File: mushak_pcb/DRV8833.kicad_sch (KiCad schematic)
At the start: 8 parts, among them U3 DRV8833PW

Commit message: Add footprints
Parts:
- C26, C27, C28: footprint (none) -> Capacitor_SMD:C_0805_2012Metric
- TP24, TP25, TP26: footprint (none) -> TestPoint:TestPoint_Pad_2.5x2.5mm
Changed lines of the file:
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@@
       (effects (font (size 1 1)) (justify left))
     )
-    (property "Footprint" "" (id 2) (at 194.31 113.03 0)
+    (property "Footprint" "TestPoint:TestPoint_Pad_2.5x2.5mm" (id 2) (at 194.31 113.03 0)
       (effects (font (size 1.27 1.27)) hide)
     )
@@
       (effects (font (size 1 1)) (justify left))
     )
-    (property "Footprint" "" (id 2) (at 194.31 107.95 0)
+    (property "Footprint" "TestPoint:TestPoint_Pad_2.5x2.5mm" (id 2) (at 194.31 107.95 0)
       (effects (font (size 1.27 1.27)) hide)
     )
@@
     (property "Reference" "C26" (id 0) (at 126.492 82.55 90))
     (property "Value" "10nF" (id 1) (at 126.492 85.09 90))
-    (property "Footprint" "" (id 2) (at 130.302 89.2048 0)
+    (property "Footprint" "Capacitor_SMD:C_0805_2012Metric" (id 2) (at 130.302 89.2048 0)
       (effects (font (size 1.27 1.27)) hide)
     )
@@
       (effects (font (size 1 1)) (justify left))
     )
-    (property "Footprint" "" (id 2) (at 194.31 110.49 0)
+    (property "Footprint" "TestPoint:TestPoint_Pad_2.5x2.5mm" (id 2) (at 194.31 110.49 0)
       (effects (font (size 1.27 1.27)) hide)
     )
@@
     (property "Reference" "C27" (id 0) (at 143.764 68.58 90))
     (property "Value" "2.2uF" (id 1) (at 143.764 71.12 90))
-    (property "Footprint" "" (id 2) (at 147.574 74.7268 0)
+    (property "Footprint" "Capacitor_SMD:C_0805_2012Metric" (id 2) (at 147.574 74.7268 0)
       (effects (font (size 1.27 1.27)) hide)
     )
@@
     (property "Reference" "C28" (id 0) (at 163.322 68.58 90))
     (property "Value" "10uF" (id 1) (at 163.322 71.12 90))
-    (property "Footprint" "" (id 2) (at 167.132 74.7268 0)
+    (property "Footprint" "Capacitor_SMD:C_0805_2012Metric" (id 2) (at 167.132 74.7268 0)
       (effects (font (size 1.27 1.27)) hide)
     )

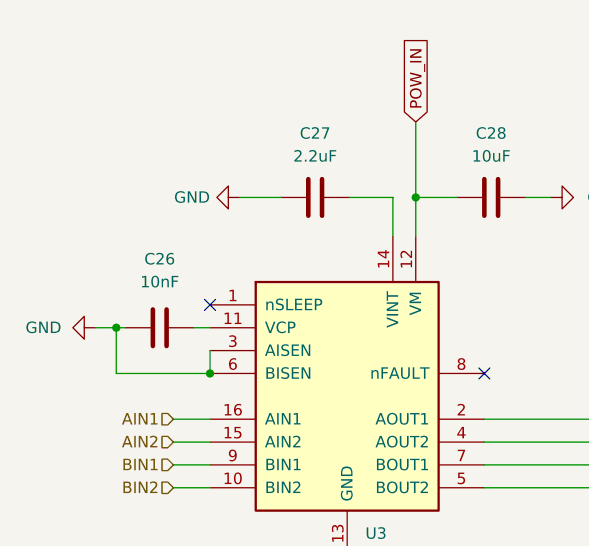
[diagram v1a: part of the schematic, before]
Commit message: Update Schematics and footprints for sensors
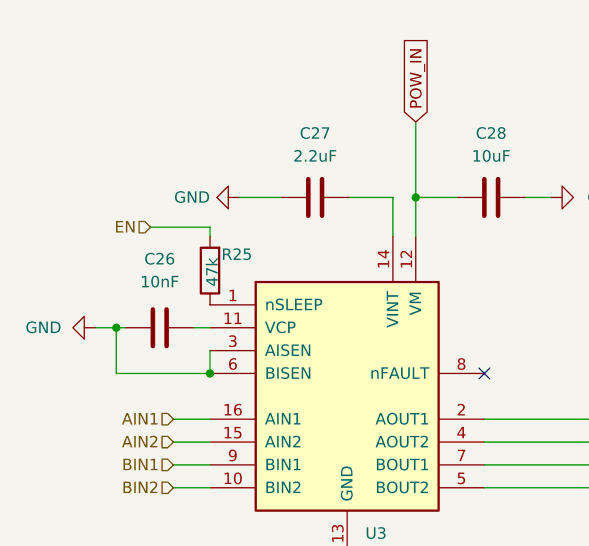
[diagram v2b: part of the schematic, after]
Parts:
- added R25: 47k, Resistor_SMD:R_0402_1005Metric, symbol Device:R
- C26, C27, C28: footprint Capacitor_SMD:C_0805_2012Metric -> Capacitor_SMD:C_0402_1005Metric
- TP23, TP24, TP25, TP26: footprint TestPoint:TestPoint_Pad_2.5x2.5mm -> TestPoint:TestPoint_Pad_1.0x1.0mm
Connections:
- net at U3.1 (nSLEEP): now also R25.1
- new net EN: R25.2
- no-connect marks 2 -> 1
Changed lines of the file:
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@@
   )
   (no_connect (at 162.56 95.25))
-  (no_connect (at 132.08 87.63))
   (wire (pts (xy 154.94 67.31) (xy 154.94 75.692))
     (stroke (width 0) (type default) (color 0 0 0 0))
@@
     (stroke (width 0) (type default) (color 0 0 0 0))
   )
+  (wire (pts (xy 132.08 78.994) (xy 132.08 80.01))
+    (stroke (width 0) (type default) (color 0 0 0 0))
+  )
   (wire (pts (xy 154.94 75.692) (xy 159.512 75.692))
     (stroke (width 0) (type default) (color 0 0 0 0))
@@
   )
   (wire (pts (xy 128.016 100.33) (xy 132.08 100.33))
+    (stroke (width 0) (type default) (color 0 0 0 0))
+  )
+  (wire (pts (xy 125.476 78.994) (xy 132.08 78.994))
     (stroke (width 0) (type default) (color 0 0 0 0))
   )
@@
     (effects (font (size 1.27 1.27)) (justify right))
   )
+  (hierarchical_label "EN" (shape input) (at 125.476 78.994 180)
+    (effects (font (size 1.27 1.27)) (justify right))
+  )
   (hierarchical_label "AIN1" (shape input) (at 128.016 100.33 180)
     (effects (font (size 1.27 1.27)) (justify right))
@@
       (effects (font (size 1 1)) (justify left))
     )
-    (property "Footprint" "TestPoint:TestPoint_Pad_2.5x2.5mm" (id 2) (at 194.31 113.03 0)
+    (property "Footprint" "TestPoint:TestPoint_Pad_1.0x1.0mm" (id 2) (at 194.31 113.03 0)
       (effects (font (size 1.27 1.27)) hide)
     )
@@
       (effects (font (size 1 1)) (justify left))
     )
-    (property "Footprint" "TestPoint:TestPoint_Pad_2.5x2.5mm" (id 2) (at 194.31 107.95 0)
+    (property "Footprint" "TestPoint:TestPoint_Pad_1.0x1.0mm" (id 2) (at 194.31 107.95 0)
       (effects (font (size 1.27 1.27)) hide)
     )
@@
     (pin "1")
   )
+  (symbol (lib_id "Device:R") (at 132.08 83.82 180) (unit 1)
+    (in_bom yes) (on_board yes)
+    (property "Reference" "R25" (id 0) (at 133.35 82.042 0)
+      (effects (font (size 1.27 1.27)) (justify right))
+    )
+    (property "Value" "47k" (id 1) (at 132.334 85.598 90)
+      (effects (font (size 1.27 1.27)) (justify right))
+    )
+    (property "Footprint" "Resistor_SMD:R_0402_1005Metric" (id 2) (at 133.858 83.82 90)
+      (effects (font (size 1.27 1.27)) hide)
+    )
+    (property "Datasheet" "~" (id 3) (at 132.08 83.82 0)
+      (effects (font (size 1.27 1.27)) hide)
+    )
+    (pin "1")
+    (pin "2")
+  )
   (symbol (lib_id "Connector:TestPoint_Alt") (at 194.31 100.33 270) (unit 1)
     (in_bom yes) (on_board yes)
@@
       (effects (font (size 1 1)) (justify left))
     )
-    (property "Footprint" "TestPoint:TestPoint_Pad_2.5x2.5mm" (id 2) (at 194.31 105.41 0)
+    (property "Footprint" "TestPoint:TestPoint_Pad_1.0x1.0mm" (id 2) (at 194.31 105.41 0)
       (effects (font (size 1.27 1.27)) hide)
     )
@@
     (property "Reference" "C26" (id 0) (at 126.492 82.55 90))
     (property "Value" "10nF" (id 1) (at 126.492 85.09 90))
-    (property "Footprint" "Capacitor_SMD:C_0805_2012Metric" (id 2) (at 130.302 89.2048 0)
+    (property "Footprint" "Capacitor_SMD:C_0402_1005Metric" (id 2) (at 130.302 89.2048 0)
       (effects (font (size 1.27 1.27)) hide)
     )
@@
       (effects (font (size 1 1)) (justify left))
     )
-    (property "Footprint" "TestPoint:TestPoint_Pad_2.5x2.5mm" (id 2) (at 194.31 110.49 0)
+    (property "Footprint" "TestPoint:TestPoint_Pad_1.0x1.0mm" (id 2) (at 194.31 110.49 0)
       (effects (font (size 1.27 1.27)) hide)
     )
@@
     (property "Reference" "C27" (id 0) (at 143.764 68.58 90))
     (property "Value" "2.2uF" (id 1) (at 143.764 71.12 90))
-    (property "Footprint" "Capacitor_SMD:C_0805_2012Metric" (id 2) (at 147.574 74.7268 0)
+    (property "Footprint" "Capacitor_SMD:C_0402_1005Metric" (id 2) (at 147.574 74.7268 0)
       (effects (font (size 1.27 1.27)) hide)
     )
@@
     (property "Reference" "C28" (id 0) (at 163.322 68.58 90))
     (property "Value" "10uF" (id 1) (at 163.322 71.12 90))
-    (property "Footprint" "Capacitor_SMD:C_0805_2012Metric" (id 2) (at 167.132 74.7268 0)
-      (effects (font (size 1.27 1.27)) hide)
-    )
+    (property "Footprint" "Capacitor_SMD:C_0402_1005Metric" (id 2) (at 167.132 74.7268 0)
+      (effects (font (size 1.27 1.27)) hide)
+    )

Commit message: changed footprints of capacitors and resistors
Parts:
- R25: footprint Resistor_SMD:R_0402_1005Metric -> Resistor_SMD:R_0201_0603Metric
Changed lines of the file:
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@@
       (effects (font (size 1.27 1.27)) (justify right))
     )
-    (property "Footprint" "Resistor_SMD:R_0402_1005Metric" (id 2) (at 133.858 83.82 90)
+    (property "Footprint" "Resistor_SMD:R_0201_0603Metric" (id 2) (at 133.858 83.82 90)
       (effects (font (size 1.27 1.27)) hide)
     )

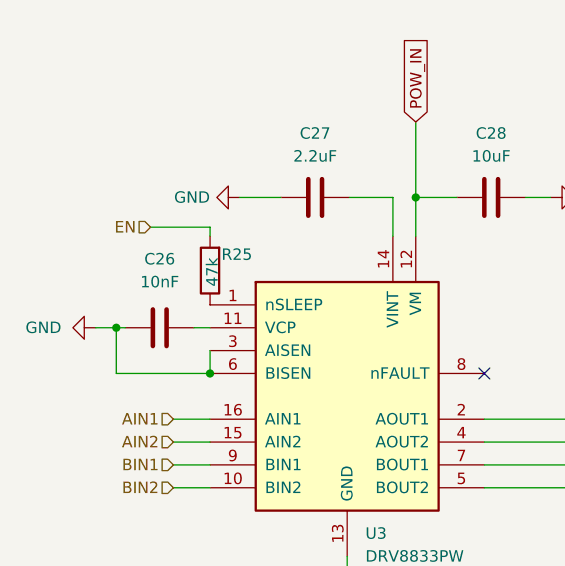
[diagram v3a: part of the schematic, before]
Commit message: made draft pcb footprint placement
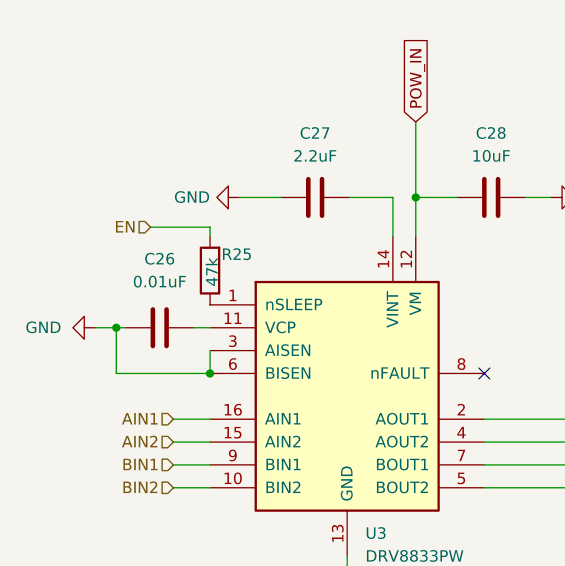
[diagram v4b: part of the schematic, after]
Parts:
- C26: value 10nF -> 0.01uF
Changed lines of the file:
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@@
     (in_bom yes) (on_board yes) (fields_autoplaced)
     (property "Reference" "C26" (id 0) (at 126.492 82.55 90))
-    (property "Value" "10nF" (id 1) (at 126.492 85.09 90))
+    (property "Value" "0.01uF" (id 1) (at 126.492 85.09 90))
     (property "Footprint" "Capacitor_SMD:C_0402_1005Metric" (id 2) (at 130.302 89.2048 0)
       (effects (font (size 1.27 1.27)) hide)

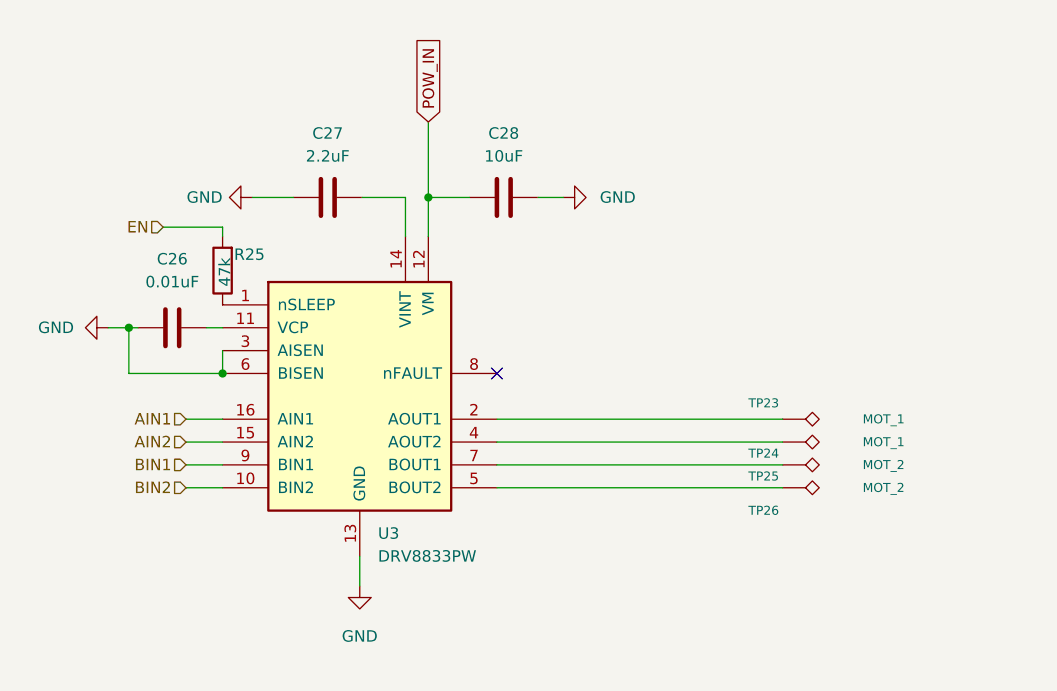
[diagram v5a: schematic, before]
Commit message: updated footprint for motors
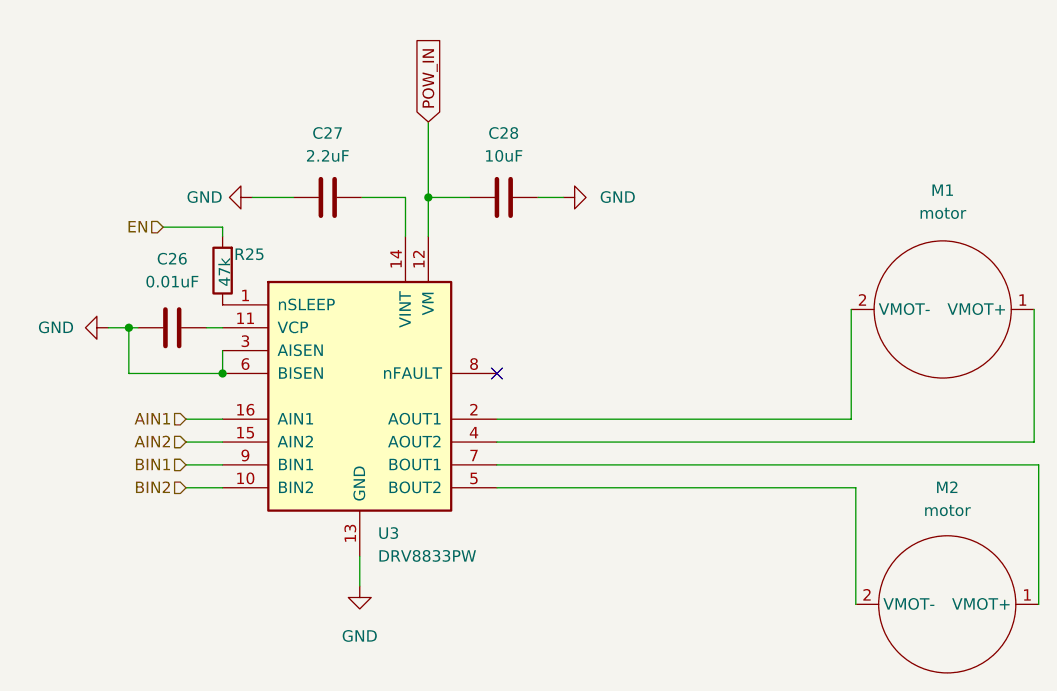
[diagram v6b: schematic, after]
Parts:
- removed TP23, TP24: MOT_1, TestPoint:TestPoint_Pad_1.0x1.0mm, symbol Connector:TestPoint_Alt
- removed TP25, TP26: MOT_2, TestPoint:TestPoint_Pad_1.0x1.0mm, symbol Connector:TestPoint_Alt
- added M1, M2: motor, mushak_mount_footprint:motor, symbol New_Library:motor
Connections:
- net at U3.5 (BOUT2): now also M2.2 (VMOT-)
- net at U3.4 (AOUT2): now also M1.1 (VMOT+)
- net at U3.2 (AOUT1): now also M1.2 (VMOT-)
- net at U3.7 (BOUT1): now also M2.1 (VMOT+)
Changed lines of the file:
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@@
     (stroke (width 0) (type default) (color 0 0 0 0))
   )
-  (wire (pts (xy 162.56 107.95) (xy 194.31 107.95))
+  (wire (pts (xy 162.56 107.95) (xy 202.438 107.95))
     (stroke (width 0) (type default) (color 0 0 0 0))
   )
@@
     (stroke (width 0) (type default) (color 0 0 0 0))
   )
-  (wire (pts (xy 162.56 100.33) (xy 194.31 100.33))
+  (wire (pts (xy 162.56 100.33) (xy 201.93 100.33))
+    (stroke (width 0) (type default) (color 0 0 0 0))
+  )
+  (wire (pts (xy 202.438 107.95) (xy 202.438 120.904))
     (stroke (width 0) (type default) (color 0 0 0 0))
   )
@@
     (stroke (width 0) (type default) (color 0 0 0 0))
   )
+  (wire (pts (xy 222.758 120.904) (xy 222.758 105.41))
+    (stroke (width 0) (type default) (color 0 0 0 0))
+  )
+  (wire (pts (xy 222.25 102.87) (xy 222.25 88.138))
+    (stroke (width 0) (type default) (color 0 0 0 0))
+  )
   (wire (pts (xy 121.666 95.25) (xy 121.666 90.17))
     (stroke (width 0) (type default) (color 0 0 0 0))
@@
     (stroke (width 0) (type default) (color 0 0 0 0))
   )
-  (wire (pts (xy 162.56 105.41) (xy 194.31 105.41))
-    (stroke (width 0) (type default) (color 0 0 0 0))
-  )
-  (wire (pts (xy 162.56 102.87) (xy 194.31 102.87))
+  (wire (pts (xy 162.56 105.41) (xy 222.758 105.41))
+    (stroke (width 0) (type default) (color 0 0 0 0))
+  )
+  (wire (pts (xy 162.56 102.87) (xy 222.25 102.87))
     (stroke (width 0) (type default) (color 0 0 0 0))
   )
   (wire (pts (xy 132.08 92.71) (xy 132.08 95.25))
+    (stroke (width 0) (type default) (color 0 0 0 0))
+  )
+  (wire (pts (xy 201.93 100.33) (xy 201.93 88.138))
     (stroke (width 0) (type default) (color 0 0 0 0))
   )
@@
     (pin "1")
   )
-  (symbol (lib_id "Connector:TestPoint_Alt") (at 194.31 107.95 270) (unit 1)
-    (in_bom yes) (on_board yes)
-    (property "Reference" "TP26" (id 0) (at 190.5 110.49 90)
-      (effects (font (size 1 1)) (justify left))
-    )
-    (property "Value" "MOT_2" (id 1) (at 203.2 107.95 90)
-      (effects (font (size 1 1)) (justify left))
-    )
-    (property "Footprint" "TestPoint:TestPoint_Pad_1.0x1.0mm" (id 2) (at 194.31 113.03 0)
-      (effects (font (size 1.27 1.27)) hide)
-    )
-    (property "Datasheet" "~" (id 3) (at 194.31 113.03 0)
-      (effects (font (size 1.27 1.27)) hide)
-    )
-    (pin "1")
-  )
   (symbol (lib_id "power:GND") (at 147.32 118.872 0) (unit 1)
     (in_bom yes) (on_board yes) (fields_autoplaced)
@@
     )
     (property "Datasheet" "" (id 3) (at 119.38 90.17 0)
-      (effects (font (size 1.27 1.27)) hide)
-    )
-    (pin "1")
-  )
-  (symbol (lib_id "Connector:TestPoint_Alt") (at 194.31 102.87 270) (unit 1)
-    (in_bom yes) (on_board yes)
-    (property "Reference" "TP24" (id 0) (at 190.5 104.14 90)
-      (effects (font (size 1 1)) (justify left))
-    )
-    (property "Value" "MOT_1" (id 1) (at 203.2 102.87 90)
-      (effects (font (size 1 1)) (justify left))
-    )
-    (property "Footprint" "TestPoint:TestPoint_Pad_1.0x1.0mm" (id 2) (at 194.31 107.95 0)
-      (effects (font (size 1.27 1.27)) hide)
-    )
-    (property "Datasheet" "~" (id 3) (at 194.31 107.95 0)
       (effects (font (size 1.27 1.27)) hide)
     )
@@
     (pin "2")
   )
-  (symbol (lib_id "Connector:TestPoint_Alt") (at 194.31 100.33 270) (unit 1)
-    (in_bom yes) (on_board yes)
-    (property "Reference" "TP23" (id 0) (at 190.5 98.552 90)
-      (effects (font (size 1 1)) (justify left))
-    )
-    (property "Value" "MOT_1" (id 1) (at 203.2 100.33 90)
-      (effects (font (size 1 1)) (justify left))
-    )
-    (property "Footprint" "TestPoint:TestPoint_Pad_1.0x1.0mm" (id 2) (at 194.31 105.41 0)
-      (effects (font (size 1.27 1.27)) hide)
-    )
-    (property "Datasheet" "~" (id 3) (at 194.31 105.41 0)
-      (effects (font (size 1.27 1.27)) hide)
-    )
-    (pin "1")
+  (symbol (lib_id "New_Library:motor") (at 212.09 88.138 0) (unit 1)
+    (in_bom yes) (on_board yes) (fields_autoplaced)
+    (property "Reference" "M1" (id 0) (at 212.09 74.93 0))
+    (property "Value" "motor" (id 1) (at 212.09 77.47 0))
+    (property "Footprint" "mushak_mount_footprint:motor" (id 2) (at 212.09 88.138 0)
+      (effects (font (size 1.27 1.27)) hide)
+    )
+    (property "Datasheet" "" (id 3) (at 212.09 88.138 0)
+      (effects (font (size 1.27 1.27)) hide)
+    )
+    (pin "1")
+    (pin "2")
   )
   (symbol (lib_id "Driver_Motor:DRV8833PW") (at 147.32 97.79 0) (unit 1)
@@
     (pin "9")
   )
+  (symbol (lib_id "New_Library:motor") (at 212.598 120.904 0) (unit 1)
+    (in_bom yes) (on_board yes) (fields_autoplaced)
+    (property "Reference" "M2" (id 0) (at 212.598 107.95 0))
+    (property "Value" "motor" (id 1) (at 212.598 110.49 0))
+    (property "Footprint" "mushak_mount_footprint:motor" (id 2) (at 212.598 120.904 0)
+      (effects (font (size 1.27 1.27)) hide)
+    )
+    (property "Datasheet" "" (id 3) (at 212.598 120.904 0)
+      (effects (font (size 1.27 1.27)) hide)
+    )
+    (pin "1")
+    (pin "2")
+  )
   (symbol (lib_id "Device:C") (at 126.492 90.17 90) (unit 1)
     (in_bom yes) (on_board yes) (fields_autoplaced)
@@
       (effects (font (size 1.27 1.27)) hide)
     )
-    (pin "1")
-  )
-  (symbol (lib_id "Connector:TestPoint_Alt") (at 194.31 105.41 270) (unit 1)
-    (in_bom yes) (on_board yes)
-    (property "Reference" "TP25" (id 0) (at 190.5 106.68 90)
-      (effects (font (size 1 1)) (justify left))
-    )
-    (property "Value" "MOT_2" (id 1) (at 203.2 105.41 90)
-      (effects (font (size 1 1)) (justify left))
-    )
-    (property "Footprint" "TestPoint:TestPoint_Pad_1.0x1.0mm" (id 2) (at 194.31 110.49 0)
-      (effects (font (size 1.27 1.27)) hide)
-    )
-    (property "Datasheet" "~" (id 3) (at 194.31 110.49 0)
-      (effects (font (size 1.27 1.27)) hide)
-    )
